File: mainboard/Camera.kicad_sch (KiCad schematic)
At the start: 11 parts, among them IC1201 TXB0102DCU, IC1202 PCA9306JK, X1201 Camera, Y1201 25 MHz

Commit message: Continue routing, add flash LEDs for the RGB camera, add PWM controller for the Display Backlight and the flash LEDs, add Polyfuse for the battery
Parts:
- R1202, R1203: mouser# (none) -> 603-RC0603FR-072K83L
- R1204: mouser# (none) -> 603-RC0603FR-07200KL
- R1205, R1206: mouser# (none) -> 603-RC0603FR-073K3L
- X1201: footprint (none) -> Connector_FFC-FPC:Amphenol_F32R-1A7x1-11024_1x24-1MP_P0.5mm_Horizontal; manf (none) -> Amphenol Aorora; manf# (none) -> F32R-1A7H1-11024; mouser# (none) -> 649-F32R-1A7H1-11024
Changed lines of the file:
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@@
 			)
 		)
-		(property "Datasheet" "~"
+		(property "Datasheet" "https://www.mouser.com/catalog/specsheets/YAGEO_PYu_RC_Group_51_RoHS_L_12.pdf"
 			(at 267.97 68.58 0)
 			(effects
@@
 			)
 		)
-		(property "mouser#" ""
+		(property "mouser#" "603-RC0603FR-073K3L"
 			(at 267.97 68.58 0)
 			(effects
@@
 			)
 		)
-		(property "Datasheet" "~"
+		(property "Datasheet" "https://www.mouser.com/catalog/specsheets/YAGEO_PYu_RC_Group_51_RoHS_L_12.pdf"
 			(at 260.35 54.61 0)
 			(effects
@@
 			)
 		)
-		(property "mouser#" ""
+		(property "mouser#" "603-RC0603FR-07200KL"
 			(at 260.35 54.61 0)
 			(effects
@@
 			)
 		)
-		(property "Footprint" ""
+		(property "Footprint" "Connector_FFC-FPC:Amphenol_F32R-1A7x1-11024_1x24-1MP_P0.5mm_Horizontal"
 			(at 31.75 88.9 0)
 			(effects
@@
 			)
 		)
-		(property "Datasheet" "~"
+		(property "Datasheet" "https://cdn.amphenol-cs.com/media/wysiwyg/files/drawing/f32r-f32j.pdf"
 			(at 31.75 88.9 0)
 			(effects
@@
 			)
 		)
-		(property "manf" ""
+		(property "manf" "Amphenol Aorora"
 			(at 31.75 88.9 0)
 			(effects
@@
 			)
 		)
-		(property "manf#" ""
+		(property "manf#" "F32R-1A7H1-11024"
 			(at 31.75 88.9 0)
 			(effects
@@
 			)
 		)
-		(property "mouser#" ""
+		(property "mouser#" "649-F32R-1A7H1-11024"
 			(at 31.75 88.9 0)
 			(effects
@@
 			)
 		)
-		(property "Datasheet" "~"
+		(property "Datasheet" "https://www.mouser.com/catalog/specsheets/YAGEO_PYu_RC_Group_51_RoHS_L_12.pdf"
 			(at 270.51 68.58 0)
 			(effects
@@
 			)
 		)
-		(property "mouser#" ""
+		(property "mouser#" "603-RC0603FR-073K3L"
 			(at 270.51 68.58 0)
 			(effects
@@
 			)
 		)
-		(property "Datasheet" "~"
+		(property "Datasheet" "https://www.mouser.com/catalog/specsheets/YAGEO_PYu_RC_Group_51_RoHS_L_12.pdf"
 			(at 218.44 68.58 0)
 			(effects
@@
 			)
 		)
-		(property "mouser#" ""
+		(property "mouser#" "603-RC0603FR-072K83L"
 			(at 218.44 68.58 0)
 			(effects
@@
 			)
 		)
-		(property "Datasheet" "~"
+		(property "Datasheet" "https://www.mouser.com/catalog/specsheets/YAGEO_PYu_RC_Group_51_RoHS_L_12.pdf"
 			(at 215.9 68.58 0)
 			(effects
@@
 			)
 		)
-		(property "mouser#" ""
+		(property "mouser#" "603-RC0603FR-072K83L"
 			(at 215.9 68.58 0)
 			(effects

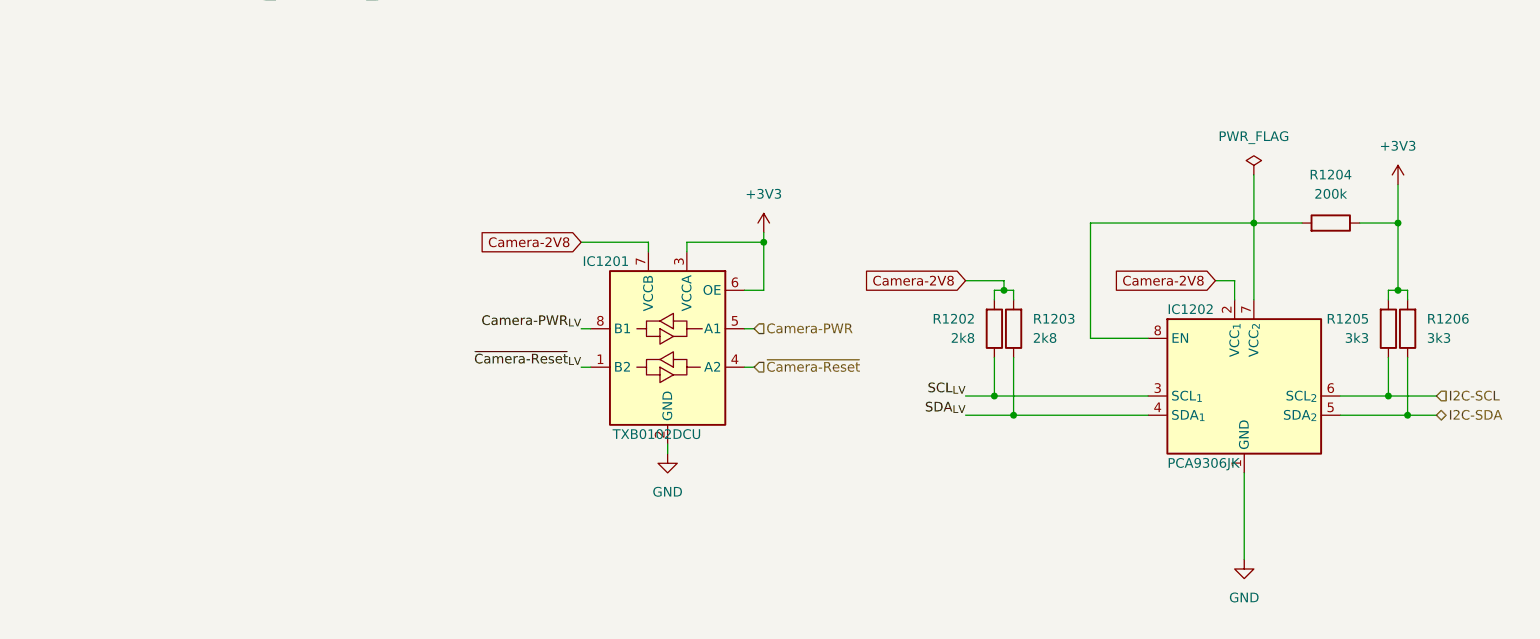
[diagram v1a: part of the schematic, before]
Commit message: Remove ADC for battery measurement and add a fuel gauge
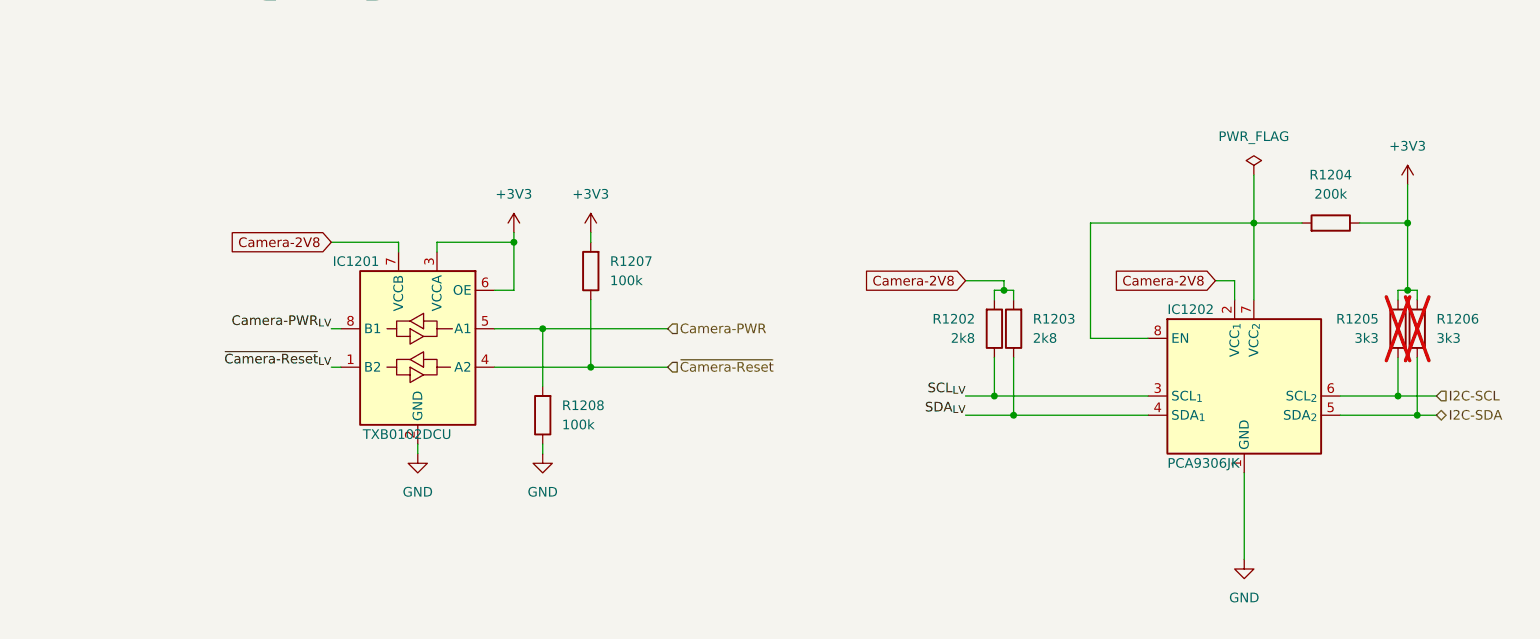
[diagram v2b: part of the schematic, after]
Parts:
- added R1207, R1208: 100k, Resistor_SMD:R_0603_1608Metric, symbol Device:R
- R1205, R1206: now not fitted; now left out of the parts list
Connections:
- net +3V3: now also R1207.2
- net Camera-PWR: now also R1208.2
- net GND: now also R1208.1
- net ~{Camera-Reset}: now also R1207.1
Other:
- moved on the sheet: IC1201

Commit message: Layout complete
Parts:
- R1201: now fitted
- renumbered R1208 to R1202, R1207 to R1203, R1202 to R1204, R1203 to R1205, R1204 to R1206, R1205 to R1207, R1206 to R1208
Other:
- moved on the sheet: C1201, IC1201, IC1202, R1202, R1203, R1204, R1205, R1206, R1207, R1208, Y1201

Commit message: Task: Issue #7
- Increase the width of the cutout for the temperature sensor
- Add missing component informations
- Fix wrong component informations

Closes: #7

Signed-off-by: Daniel Kampert <DanielKampert@kampis-elektroecke.de>
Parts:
- R1201: mouser# 652-CR0603-J/-000ELF -> 652-CR1206-J/-000ELF
- R1206: manf# RC0603FR-07200KL -> RC0603FR-073K3L
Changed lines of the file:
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@@
 			)
 		)
-		(property "manf#" "RC0603FR-07200KL"
+		(property "manf#" "RC0603FR-073K3L"
 			(at 257.81 77.47 0)
 			(effects
@@
 			)
 		)
-		(property "mouser#" "652-CR0603-J/-000ELF"
+		(property "mouser#" "652-CR1206-J/-000ELF"
 			(at 59.69 63.5 0)
 			(effects

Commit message: Bug: Fixing several component issues
Closes: #17
Closes: #16
Closes: #15
Closes: #14
Closes: #13
Closes: #12

Signed-off-by: Daniel Kampert <danielkampert@kampis-elektroecke.de>
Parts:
- IC1201: manf# TXB0102DCUT -> TXB0102DCUR; mouser# 595-TXB0102DCUT -> 595-TXB0102DCUR
- Y1201: manf ASDDV-25.000MHz-LC-T3 -> ABRACON; manf# ABRACON -> ASDDV-25.000MHz-LC-T3
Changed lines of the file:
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@@
 			)
 		)
-		(property "manf" "ASDDV-25.000MHz-LC-T3"
+		(property "manf" "ABRACON"
 			(at 215.9 129.54 0)
 			(effects
@@
 			)
 		)
-		(property "manf#" "ABRACON"
+		(property "manf#" "ASDDV-25.000MHz-LC-T3"
 			(at 215.9 129.54 0)
 			(effects
@@
 			)
 		)
-		(property "manf#" "TXB0102DCUT"
+		(property "manf#" "TXB0102DCUR"
 			(at 139.7 87.63 0)
 			(effects
@@
 			)
 		)
-		(property "mouser#" "595-TXB0102DCUT"
+		(property "mouser#" "595-TXB0102DCUR "
 			(at 139.7 87.63 0)
 			(effects

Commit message: Prepare release 1.0.2
Signed-off-by: Daniel Kampert <DanielKampert@kampis-elektroecke.de>
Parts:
- IC1201: mouser# 595-TXB0102DCUR -> 595-TXB0102DCUR
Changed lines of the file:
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@@
 			)
 		)
-		(property "mouser#" "595-TXB0102DCUR "
+		(property "mouser#" "595-TXB0102DCUR"
 			(at 139.7 87.63 0)
 			(effects

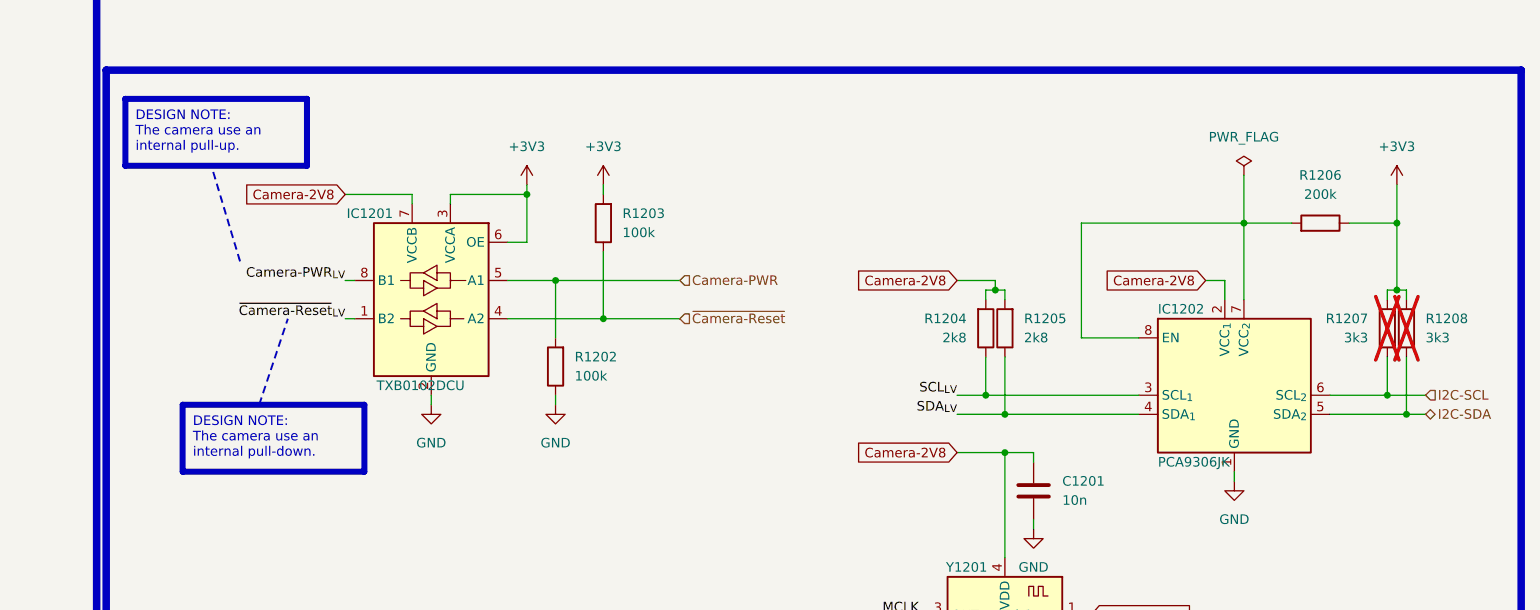
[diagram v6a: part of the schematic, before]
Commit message: Changed: Fix different minor assembly ToDos
Signed-off-by: Daniel Kampert <DanielKampert@kampis-elektroecke.de>
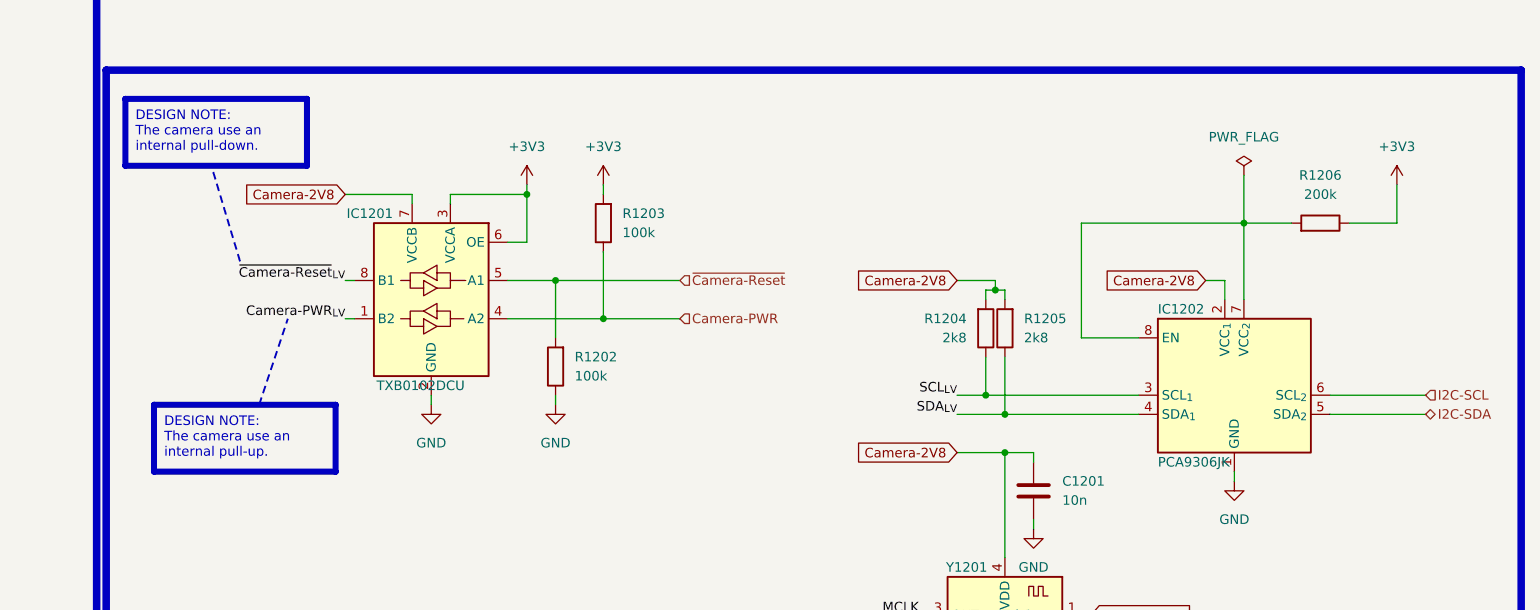
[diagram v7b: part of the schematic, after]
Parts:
- removed R1207, R1208: 3k3, Resistor_SMD:R_0603_1608Metric, symbol Device:R
- R1204, R1205: manf# RC0603FR-072K83L -> RC0603FR-072K8L; mouser# 603-RC0603FR-072K83L -> 603-RC0603FR-072K8L
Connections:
- net Camera-PWR: now also IC1201.4 (A2), R1203.1; no longer IC1201.5 (A1), R1202.2
- net Camera-PWR_{LV}: now also IC1201.1 (B2); no longer IC1201.8 (B1)
- net ~{Camera-Reset}: now also IC1201.5 (A1), R1202.2; no longer IC1201.4 (A2), R1203.1
- net ~{Camera-Reset}_{LV}: now also IC1201.8 (B1); no longer IC1201.1 (B2)

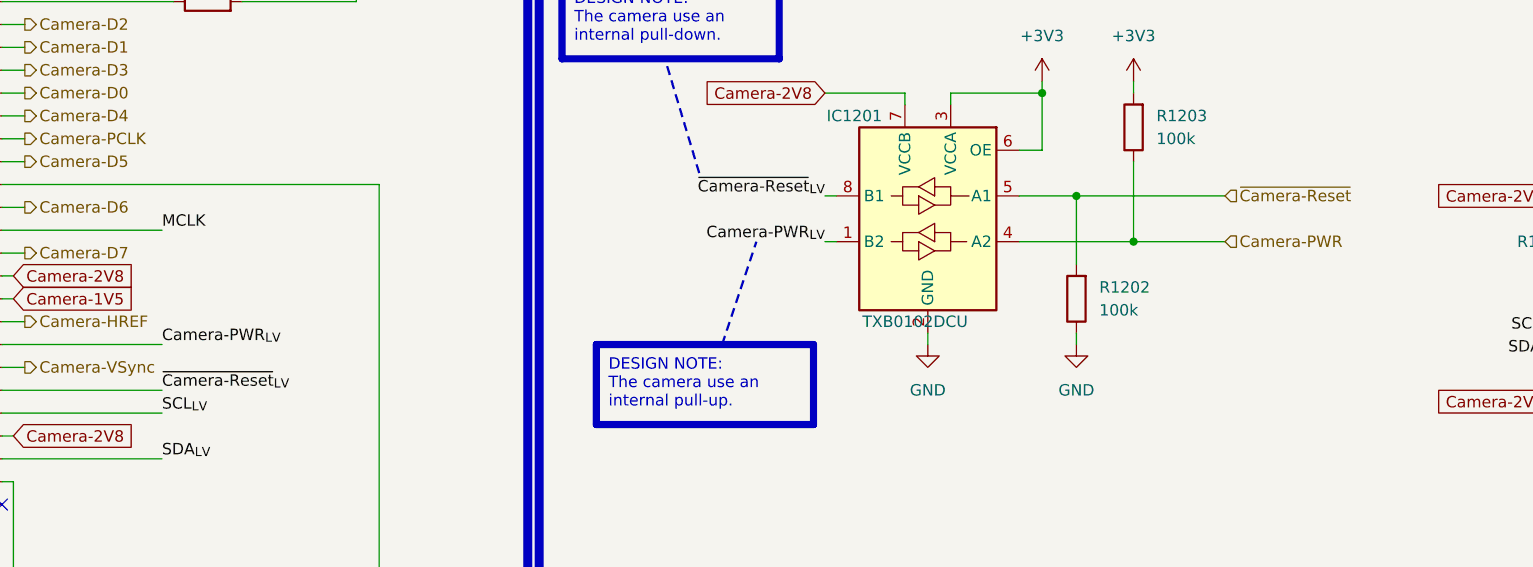
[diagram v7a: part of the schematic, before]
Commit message: Removed: Remove camera PWD signal from camera power supply enable
- The camera PWD signal is now used as a separate signal
- Solves incompatible signal levels for both enable pins
- Fix DRC issues

Signed-off-by: Daniel Kampert <DanielKampert@kampis-elektroecke.de>
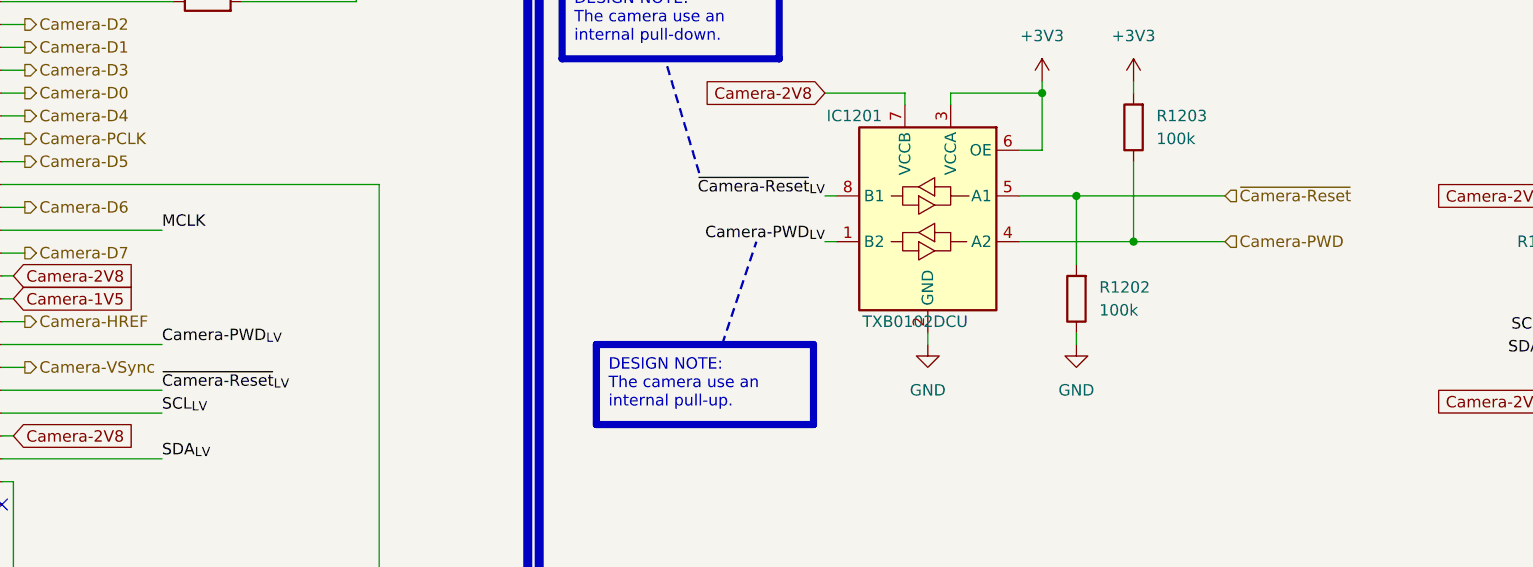
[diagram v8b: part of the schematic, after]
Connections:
- net Camera-PWR renamed Camera-PWD
- net Camera-PWR_{LV} renamed Camera-PWD_{LV}
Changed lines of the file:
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@@
 		)
 	)
-	(label "Camera-PWR_{LV}"
+	(label "Camera-PWD_{LV}"
 		(at 54.61 101.6 0)
 		(effects
@@
 		)
 	)
-	(label "Camera-PWR_{LV}"
+	(label "Camera-PWD_{LV}"
 		(at 128.27 90.17 180)
 		(effects
@@
 		)
 	)
-	(hierarchical_label "Camera-PWR"
+	(hierarchical_label "Camera-PWD"
 		(shape input)
 		(at 172.72 90.17 0)
